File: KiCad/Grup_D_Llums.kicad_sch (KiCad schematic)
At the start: 0 parts

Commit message: Raiz main creada
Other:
- added sheet Sheet_a (Sheet_a.kicad_sch)
- added sheet Sheet_b (Sheet_b.kicad_sch)
- added sheet Sheet_c (Sheet_c.kicad_sch)
- added sheet Sheet_d (Sheet_d_c.kicad_sch)
- added sheet Sheet_e (Sheet_e_c.kicad_sch)
- added sheet Sheet_f (Sheet_f_c.kicad_sch)
- title: (none) -> edd-project-grup-dimecres-dc_d_llums

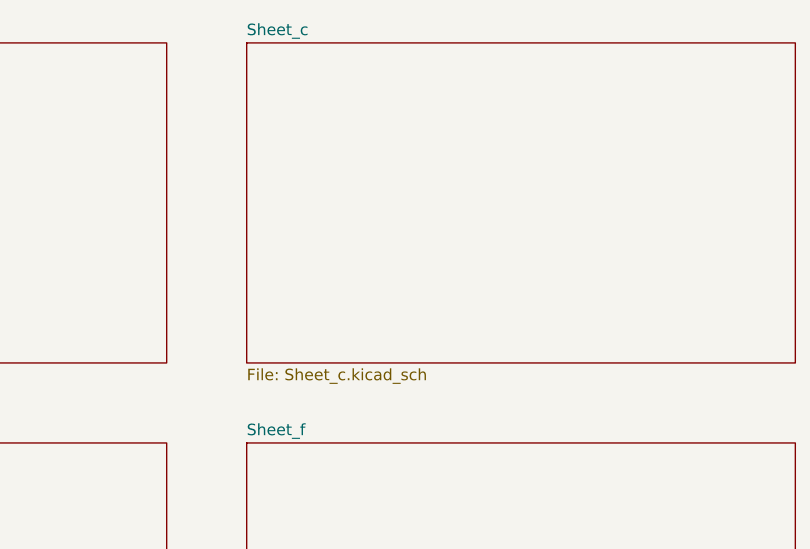
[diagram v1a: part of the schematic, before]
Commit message: Implementacio Drivers Motor Neteja fars
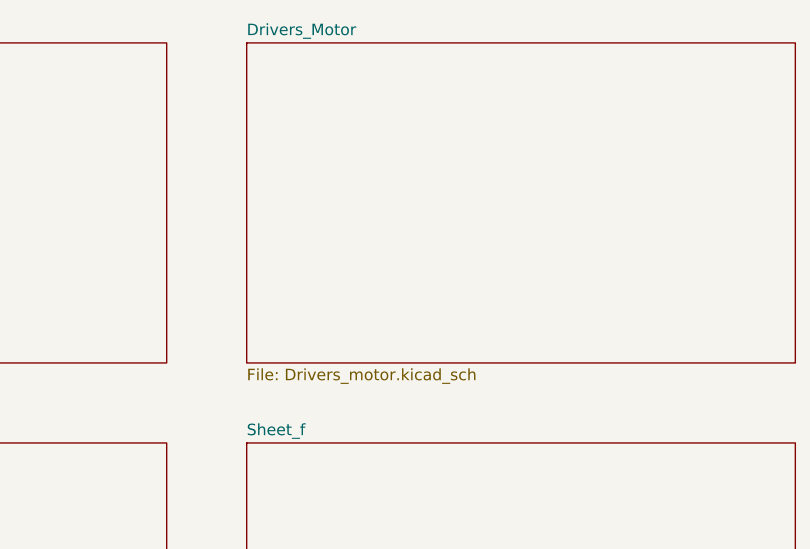
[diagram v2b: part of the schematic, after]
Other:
- sheet Sheet_c renamed Drivers_Motor
- sheet Drivers_Motor: file Sheet_c.kicad_sch -> Drivers_motor.kicad_sch
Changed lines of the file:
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@@
 			(color 0 0 0 0.0000)
 		)
-		(property "Sheetname" "Sheet_c"
+		(property "Sheetname" "Drivers_Motor"
 			(at 161.29 25.9584 0)
 			(effects
@@
 			)
 		)
-		(property "Sheetfile" "Sheet_c.kicad_sch"
+		(property "Sheetfile" "Drivers_motor.kicad_sch"
 			(at 161.29 62.8146 0)
 			(effects

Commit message: Solucionando problemas del esquematic
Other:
- sheet Sheet_a renamed Alimentacio
- sheet Sheet_b renamed Transceptor_CAN
- sheet Alimentacio: file Sheet_a.kicad_sch -> Alimentacio.kicad_sch
- sheet Transceptor_CAN: file Sheet_b.kicad_sch -> Transceptor_CAN.kicad_sch
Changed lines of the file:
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@@
 			(project "Grup_D_Llums"
 				(path "/88ef36bc-9439-47f2-adb5-e1da6bb8c9dd"
-					(page "5")
+					(page "7")
 				)
 			)
@@
 			(project "Grup_D_Llums"
 				(path "/88ef36bc-9439-47f2-adb5-e1da6bb8c9dd"
-					(page "4")
+					(page "5")
 				)
 			)
@@
 			(color 0 0 0 0.0000)
 		)
-		(property "Sheetname" "Sheet_a"
+		(property "Sheetname" "Alimentacio"
 			(at 24.13 25.9584 0)
 			(effects
@@
 			)
 		)
-		(property "Sheetfile" "Sheet_a.kicad_sch"
+		(property "Sheetfile" "Alimentacio.kicad_sch"
 			(at 24.13 62.8146 0)
 			(effects
@@
 			(color 0 0 0 0.0000)
 		)
-		(property "Sheetname" "Sheet_b"
+		(property "Sheetname" "Transceptor_CAN"
 			(at 91.44 25.9584 0)
 			(effects
@@
 			)
 		)
-		(property "Sheetfile" "Sheet_b.kicad_sch"
+		(property "Sheetfile" "Transceptor_CAN.kicad_sch"
 			(at 91.44 62.8146 0)
 			(effects
@@
 			(project "Grup_D_Llums"
 				(path "/88ef36bc-9439-47f2-adb5-e1da6bb8c9dd"
-					(page "3")
+					(page "4")
 				)
 			)
